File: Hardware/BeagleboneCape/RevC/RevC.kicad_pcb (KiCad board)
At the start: 2 copper layers, 54.6 x 86.4 mm, 6 parts, among them P1 CONN_02X04, P2 CONN_01X12, P8 BeagleBone_Black_Header, P9 BeagleBone_Black_Header

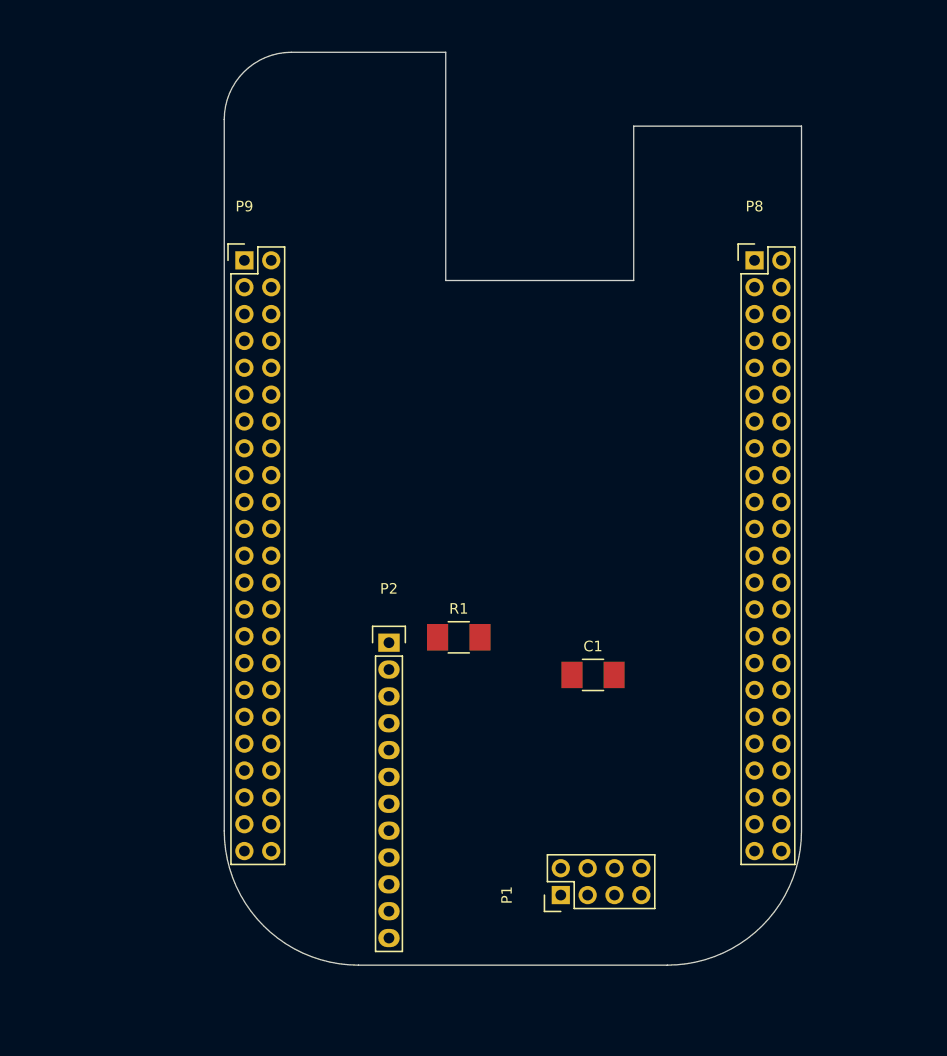
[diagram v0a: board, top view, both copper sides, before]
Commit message: initial mockup of board layout, removed 8 pin connector in favour of the single-module board
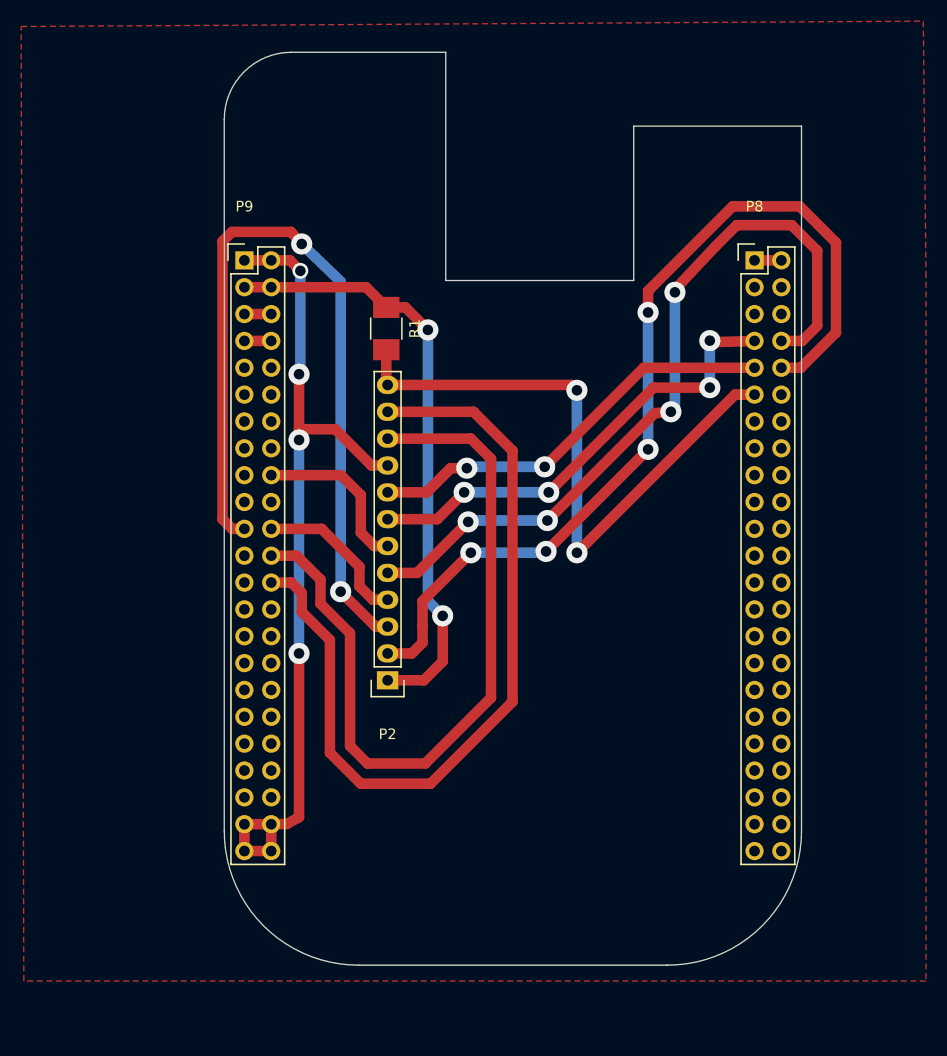
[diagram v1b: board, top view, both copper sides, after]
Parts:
- removed C1: C, Capacitors_SMD:C_1210_HandSoldering
- removed P1: CONN_02X04, Pin_Headers:Pin_Header_Straight_2x04
- moved R1 30.0 mm to (129.8, 68.8), turned to 270 degrees
- moved P2 3.56 mm to (129.9, 102.1), turned to 180 degrees
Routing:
- net CSN_MEM: track 0.00 -> 87.5 mm, vias 0 -> 4
- net GNDD: track 0.00 -> 83.2 mm, vias 0 -> 4
- net UART_RX: track 0.00 -> 78.3 mm
- net MISO: track 0.00 -> 77.4 mm, vias 0 -> 2
- net IRQ_RADIO: track 0.00 -> 72.5 mm, vias 0 -> 4
- net UART_TX: track 0.00 -> 72.3 mm
- net DETECT: track 0.00 -> 60.3 mm, vias 0 -> 2
- net +3V3: track 0.00 -> 56.9 mm, vias 0 -> 2
- net CSN_RADIO: track 0.00 -> 44.4 mm, vias 0 -> 4
- net CE_RADIO: track 0.00 -> 42.8 mm, vias 0 -> 2
- net MOSI: track 0.00 -> 15.9 mm
- net SCK: track 0.00 -> 15.8 mm
- net SYS_5V: track 0.00 -> 2.54 mm
- net +5V: track 0.00 -> 2.54 mm
- added copper zone on F.Cu, net GNDD
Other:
- net class Default: trace_width 0.25 -> 1; via_dia 0.6 -> 2; via_drill 0.4 -> 1
- rule trace_min: 0.2 -> 0.4

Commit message: updated layout to include radio header thanks to new layout tweaks
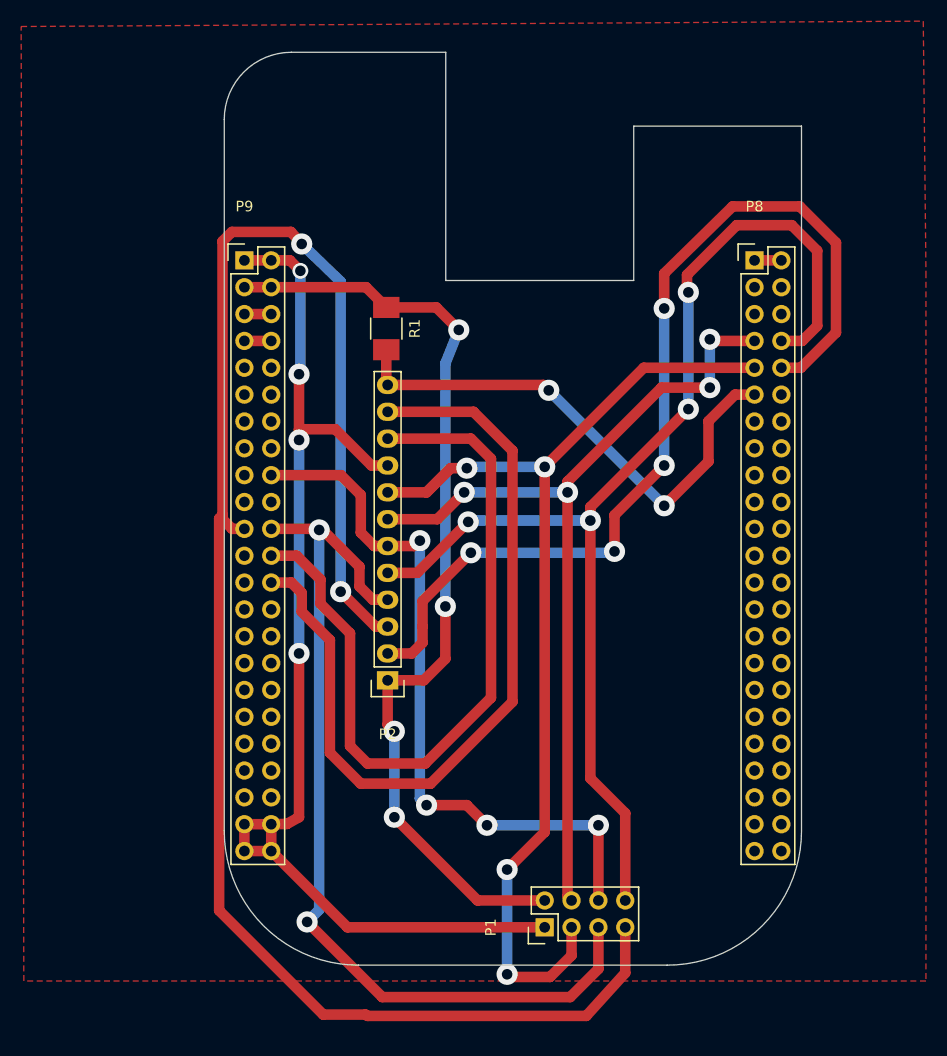
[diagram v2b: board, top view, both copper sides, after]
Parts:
- added P1: CONN_02X04, Pin_Headers:Pin_Header_Straight_2x04, F.Cu at (144.8, 125.5)
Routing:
- net MISO: track 77.4 -> 163.6 mm
- net SCK: track 15.8 -> 89.2 mm, vias 0 -> 2
- net CE_RADIO: track 42.8 -> 102.0 mm, vias 2 -> 4
- net MOSI: track 15.9 -> 68.6 mm, vias 0 -> 4
- net IRQ_RADIO: track 72.5 -> 112.0 mm
- net CSN_RADIO: track 44.4 -> 83.9 mm
- net +3V3: track 56.9 -> 90.3 mm, vias 2 -> 4
- net GNDD: track 83.2 -> 112.1 mm
- net DETECT: track 60.3 -> 49.9 mm
- net CSN_MEM: track 87.5 -> 91.3 mm

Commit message: updated board layout and exported svg files
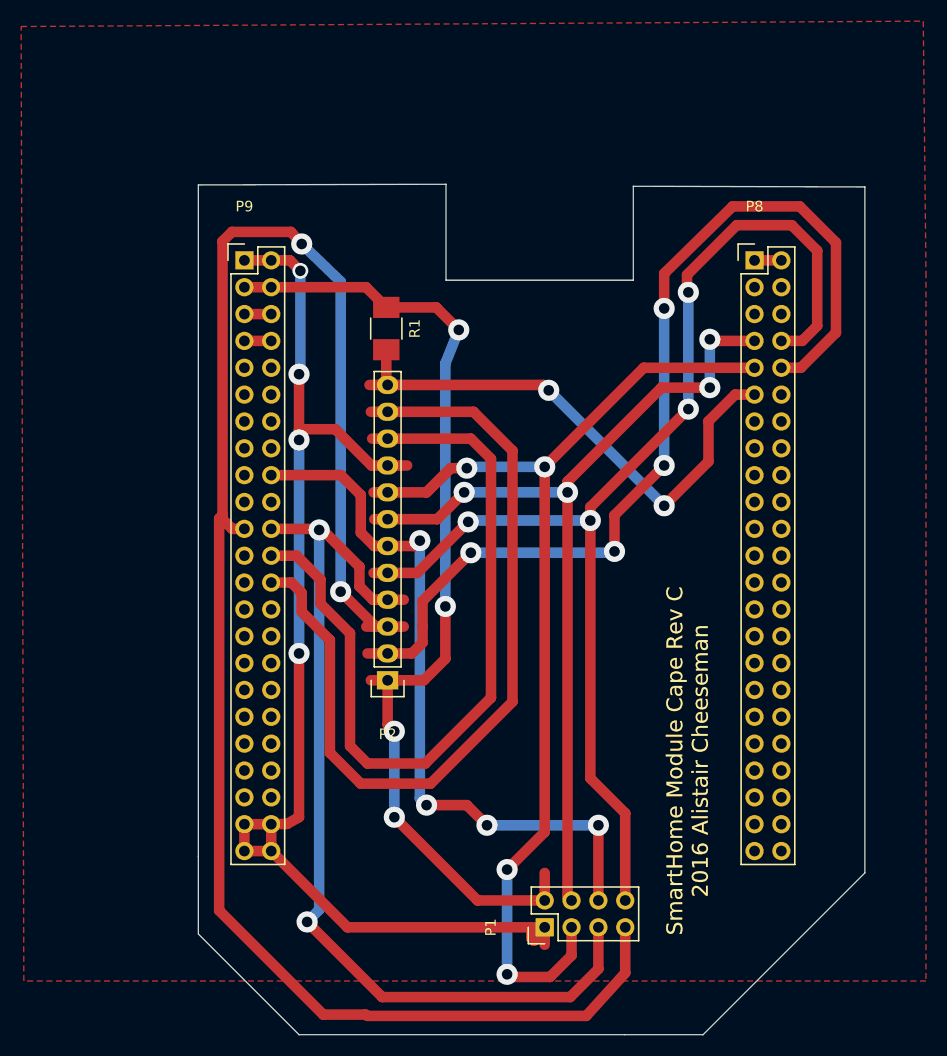
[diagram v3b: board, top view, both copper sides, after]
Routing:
- net GNDD: track 112.1 -> 117.6 mm
- net +3V3: track 90.3 -> 94.5 mm
- net MISO: track 163.6 -> 167.1 mm
- net CSN_MEM: track 91.3 -> 93.2 mm
- net DETECT: track 49.9 -> 51.6 mm
- net UART_RX: track 78.3 -> 79.9 mm
- net SCK: track 89.2 -> 90.7 mm
- net UART_TX: track 72.3 -> 73.7 mm
- net IRQ_RADIO: track 112.0 -> 113.4 mm
- net CE_RADIO: track 102.0 -> 103.3 mm
- net CSN_RADIO: track 83.9 -> 85.1 mm
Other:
- board size 54.6 x 86.4 mm -> 63.1 x 80.5 mm
- board text added: "SmartHome Module Cape Rev C 2016 Alistair Cheeseman"
